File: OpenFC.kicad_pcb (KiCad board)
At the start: 8 copper layers, 28.4 x 27.6 mm, 214 parts, among them J1 5V, J10 5V, J11 5V, J12 5V, J13 5V, J14 5V, J15 5V, J16 5V, J17 5V, J18 5V, J19 5V, J2 5V, J20 5V, J21 5V, J22 5V, J23 5V, J24 5V, J25 5V, J26 5V, J27 5V, J28 5V, J29 5V, J3 5V, J30 5V, J31 5V, J32 5V, J33 5V, J34 5V, J35 5V, J36 5V, J38 5V, J39 5V, J4 5V, J40 5V, J42 5V, J43 5V, J44 5V, J45 5V, J46 5V, J47 5V, J48 5V, J49 5V, J5 5V, J50 5V, J53 5V, J56 5V, J6 5V, J7 5V, J8 5V, J9 5V, P1 SM08B-SRSS-TB(LF)(SN), Q7 DMN1150UFB-7B, U1 SM06B-SRSS-TB(LF)(SN), U10 GD25Q256EWIGR, U12 WL9005D4-33, U13 TPS746-3.3DRV, U14 LSM6DSV16XTR, U15 XL-1010RGBC-WS2812B, U16 XL-1010RGBC-WS2812B, U17 XL-1010RGBC-WS2812B, U18 XL-1010RGBC-WS2812B, U19 XL-1010RGBC-WS2812B, U2 ESP32-C3FH4, U20 SX1281IMLTRT, U21 TPS746-3.3DRV, U22 XL-1010RGBC-WS2812B, U23 XL-1010RGBC-WS2812B, U24 XL-1010RGBC-WS2812B, U25 XL-1010RGBC-WS2812B, U26 XL-1010RGBC-WS2812B, U27 XL-1010RGBC-WS2812B, U28 XL-1010RGBC-WS2812B, U29 XL-1010RGBC-WS2812B, U3 XL-1010RGBC-WS2812B, U30 BMP388, U32 RP2354A, U33 TPS2116DRLR, U34 TS2306A 240GF MSM 9_C2976675, U35 STM32G431KBUx, U4 XL-1010RGBC-WS2812B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

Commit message: Ordered first revision
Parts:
- removed C61, C64, C65, C66: 100n, Capacitor_SMD:C_0402_1005Metric
- removed D8: LED_1_Green, LED_SMD:LED_0603_1608Metric
- removed R21: 33R, Resistor_SMD:R_0402_1005Metric
- removed U21: TPS746-3.3DRV, Package_SON:WSON-6-1EP_2x2mm_P0.65mm_EP1x1.6mm
- removed X2: Q22FA12800519, lib:CRYSTAL-SMD_4P-L2.0-W1.6-BL
- added D7: LED_1_Green, LED_SMD:LED_0603_1608Metric, F.Cu at (57.0, 105.9)
- added OSC1: OW7EL89CENUNFAYLC-52M, lib:OSC-SMD_4P-L2.0-W1.6-BL_TXC_7Z, F.Cu at (70.2, 114.3)
- added Q1: DMN1150UFB-7B, lib:DFN-3L_L1.0-W0.6-P0.65-BR, F.Cu at (58.0, 105.8)
- added R12: 200R, Resistor_SMD:R_0402_1005Metric, B.Cu at (56.5, 104.7)
- added U11: LP5900SDX-1.8/NOPB, lib:WSON-6_L2.5-W2.2-P0.65-BL-EP, B.Cu at (58.4, 106.5)
- C11, C44, C49, C75, L1, Q7, R2, R36: moved to F.Cu
- C19, C36, C45, D21, R14, R15: moved to B.Cu
- C59: value 100n -> 15p; moved to F.Cu
- FL1, FL2: value 2450FM07D0034T -> DEA102700LT-6307A2
- R17, R18: value 22R -> 30R
- R19, R4: value 33R -> 30R
- R23, R24: value 5.1k -> 6.8k
- moved R29 20.2 mm to (56.4, 102.9), turned to 180 degrees
- moved C49 20.1 mm to (50.9, 120.2), turned to -135 degrees
- moved R31 17.1 mm to (60.0, 116.6), turned to -90 degrees
- moved L4 16.9 mm to (65.8, 115.6), turned to 0 degrees
- moved R16 16.4 mm to (59.5, 118.0)
- moved C37 15.4 mm to (62.5, 117.6), turned to 180 degrees
- moved R34 13.6 mm to (68.0, 102.1), turned to 90 degrees
- moved C39 13.1 mm to (60.0, 114.8), turned to 90 degrees
- moved R22 13.0 mm to (56.4, 102.0), turned to 0 degrees
- moved R10 12.4 mm to (67.1, 102.1), turned to 90 degrees
- moved C40 12.2 mm to (64.5, 113.4), turned to 180 degrees
- moved U7 11.6 mm to (62.3, 115.4), turned to -90 degrees
- moved R37 11.3 mm to (57.9, 104.2), turned to 0 degrees
- moved R5 9.69 mm to (65.3, 115.9), turned to 180 degrees
- moved C45 9.43 mm to (64.3, 105.0), turned to 0 degrees
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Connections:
- net +3.3V_GYRO renamed +1.8V_GYRO
- C59 pad 1: +3.3V -> GND
- C59 pad 2: GND -> Net-(OSC1-Out_Put)
- C60 pad 1: +3.3V -> +3.3V_ELRS
- P1 pad 10: unconnected-(P1-Pad10) -> GND
- P1 pad 9: unconnected-(P1-Pad9) -> GND
- U1 pad 7: unconnected-(U1-Pad7) -> GND
- U1 pad 8: unconnected-(U1-Pad8) -> GND
- U2 pad 24: /ELRS/MOSI -> unconnected-(U2-SPIQ-Pad24)
- U2 pad 4: unconnected-(U2-XTAL_32K_P-Pad4) -> /ELRS/DIO
- U20 pad 4: Net-(U20-XTA) -> Net-(OSC1-Out_Put)
- U20 pad 6: Net-(U20-XTB) -> unconnected-(U20-XTB-Pad6)
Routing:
- net /OSD/OSD_TX: track 1.46 -> 35.7 mm, vias 1 -> 2
- net GND: track 124.4 -> 92.4 mm, vias 91 -> 80
- net +12V: track 9.12 -> 40.4 mm, vias 4 -> 6
- net Net-(D5-A): track 33.5 -> 5.62 mm, vias 2 -> 1
- net /ELRS/ESP_BOOT0: track 1.36 -> 25.5 mm, vias 1 -> 3
- net +BATT: track 70.4 -> 46.8 mm, vias 7 -> 6
- net +5V_BUCK: track 24.2 -> 45.9 mm, vias 5 -> 8
- net Net-(D6-A): track 28.7 -> 7.34 mm, vias 2 -> 1
- net /ELRS/ESP8285_EN: track 2.11 -> 19.9 mm, vias 1 -> 2
- net /RP2350A/LED0: track 2.06 -> 18.2 mm, vias 1 -> 2
- net Net-(Q7-G): track 16.0 -> 1.97 mm, vias 2 -> 0
- net /RP2350A/Motor4: track 36.5 -> 25.1 mm, vias 2 -> 3
- net /RP2350A/D-_C: track 2.47 -> 13.5 mm
- net /I2C_SCL: track 29.9 -> 20.5 mm
- net /PADS/SBUS: track 23.3 -> 15.3 mm, vias 2 -> 3
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- added copper zone on In3.Cu, net +3.3V_ELRS
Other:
- board size 28.4 x 27.6 mm -> 27.6 x 27.6 mm
- board text added: "LN4 = Signal"
- board text added: "OPENFC"
- board text added: "power?"
- board text removed: "LN4 = GND"
- board text removed: "antenna"
- board text removed: "break me"

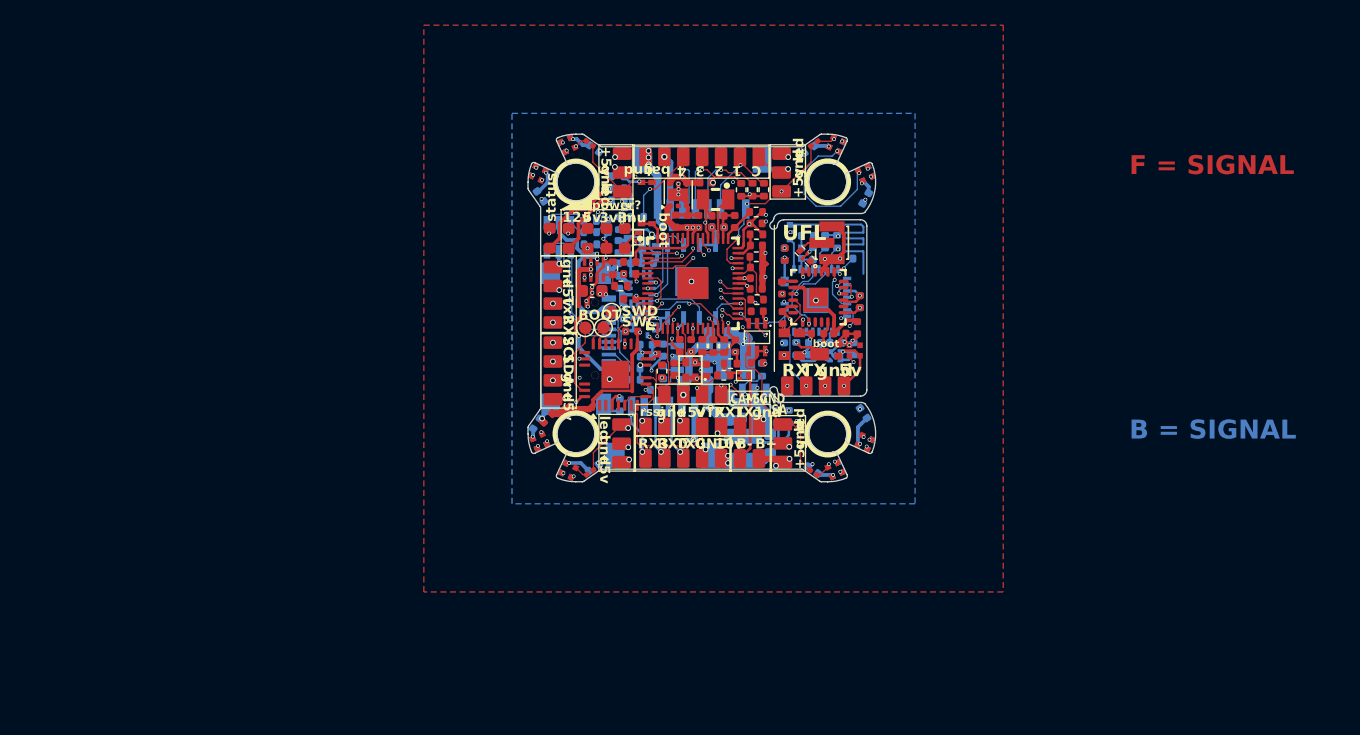
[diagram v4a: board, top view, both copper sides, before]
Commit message: Switched to RP2354B for V2 of the FC for more IO. I want to try implement OSD on PIO state machine. I know BF already uses all of them but it should be possible and then later try to combine it witht the WS2812 protocol PIO2. If anybody here has any experience with analog OSD generation let me know, I just want to make a circuit that would allow further software development later. The reason I want to do it this way is it's cheap BOM<1 euro and low footprint, just 2 2x2 IC's and some passives.
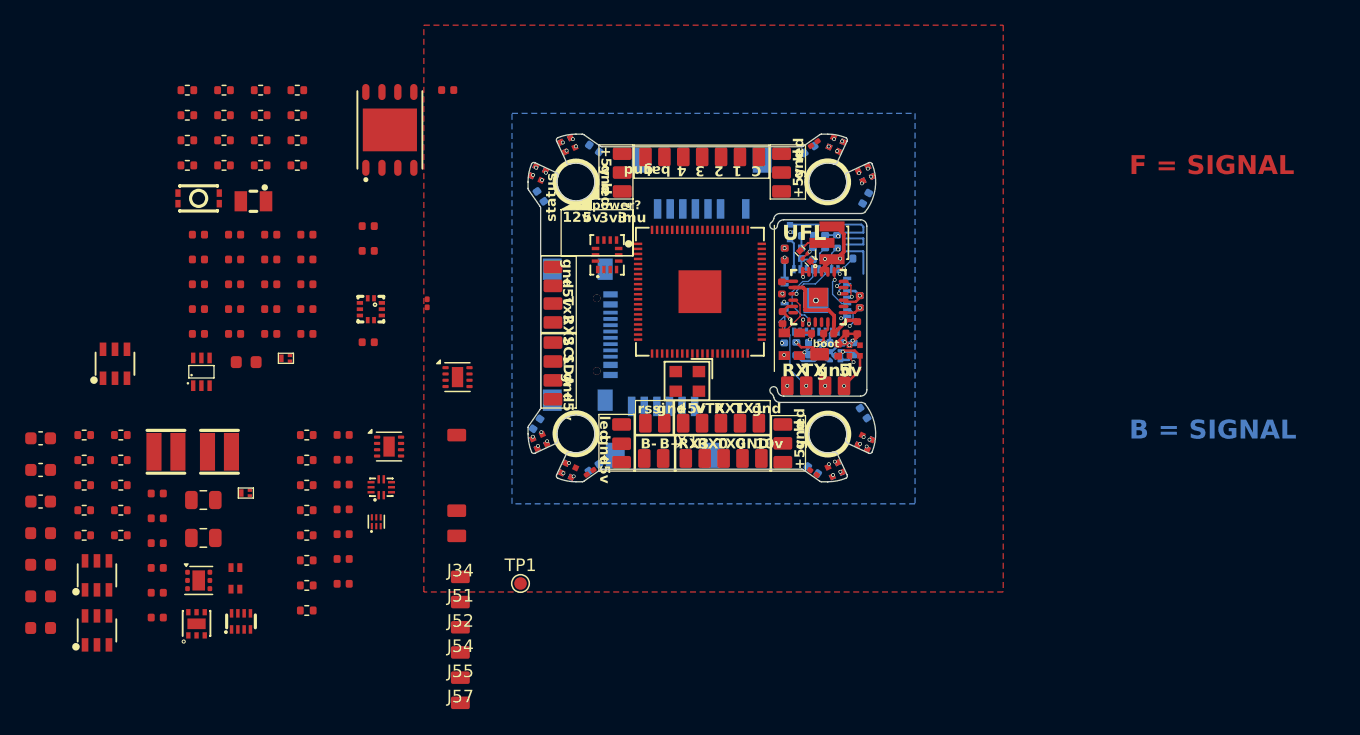
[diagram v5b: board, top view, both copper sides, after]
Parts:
- removed C10, C15, C2, C20, C24, C25, C26, C27, C28, C29, C30, C31, C4, C42, C44, C69: 100n, Capacitor_SMD:C_0402_1005Metric
- removed C21, C22, C23, C6: 4.7uF, Capacitor_SMD:C_0402_1005Metric
- removed C3: 15p, Capacitor_SMD:C_0402_1005Metric
- removed D2: USBLC6-2SC6, lib:SOT-23-6_L2.9-W1.6-P0.95-LS2.8-BL
- removed L2: AOTA-B201610S3R3-101-T, lib:IND-SMD_L2.0-W1.6_AOTA-B201610S3R3-101-T
- removed R10, R23, R24, R34, R36, R37: 6.8k, Resistor_SMD:R_0402_1005Metric
- removed R11, R25, R26: 10k, Resistor_SMD:R_0402_1005Metric
- removed R17, R18, R19: 30R, Resistor_SMD:R_0402_1005Metric
- removed R20: 200R, Resistor_SMD:R_0402_1005Metric
- removed R44, R45: 5.1k, Resistor_SMD:R_0402_1005Metric
- removed R50: 100k, Resistor_SMD:R_0402_1005Metric
- removed TP2, TP3: TestPoint, TestPoint:TestPoint_Pad_D1.0mm
- removed U10: GD25Q256EWIGR, lib:WSON-8_L6.0-W5.0-P1.27-TL-EP
- removed U11: LP5900SDX-1.8/NOPB, lib:WSON-6_L2.5-W2.2-P0.65-BL-EP
- removed U32: RP2354A, lib:QFN-60_L7.0-W7.0-P0.40-TL-EP3.4
- removed U34: TS2306A 240GF MSM 9_C2976675, lib:SW-SMD_4P-L3.0-W2.0-P0.85-LS3.5
- removed USB2: TYPE-C 16P QTWT, lib:USB-TYPE-C-SMD_TYPE-C-16P-QTWT
- removed X3: OT4EL89CJI-111YLC-12M, lib:OSC-SMD_4P-L1.6-W1.2-BL-1
- added C61: 100n, Capacitor_SMD:C_0402_1005Metric, F.Cu at (34.6, 123.5)
- added C62: 100n, Capacitor_SMD:C_0402_1005Metric, F.Cu at (34.6, 125.5)
- added C63: 100n, Capacitor_SMD:C_0402_1005Metric, F.Cu at (34.6, 127.4)
- added C64: 100n, Capacitor_SMD:C_0402_1005Metric, F.Cu at (34.6, 129.4)
- added C65: 100n, Capacitor_SMD:C_0402_1005Metric, F.Cu at (34.6, 131.4)
- added C66: 100n, Capacitor_SMD:C_0402_1005Metric, F.Cu at (34.6, 133.3)
- added C67: 4.7uF, Capacitor_SMD:C_0402_1005Metric, F.Cu at (23.1, 105.6)
- added C68: 4.7uF, Capacitor_SMD:C_0402_1005Metric, F.Cu at (23.1, 107.6)
- added C70: 100n, Capacitor_SMD:C_0402_1005Metric, F.Cu at (23.1, 109.6)
- added C72: 100n, Capacitor_SMD:C_0402_1005Metric, F.Cu at (23.1, 113.5)
- added C73: 20p, Capacitor_SMD:C_0402_1005Metric, F.Cu at (26.0, 105.6)
- added C74: 20p, Capacitor_SMD:C_0402_1005Metric, F.Cu at (26.0, 107.6)
- added C77: 4.7uF, Capacitor_SMD:C_0402_1005Metric, F.Cu at (26.0, 113.5)
- added C78: 100n, Capacitor_SMD:C_0402_1005Metric, F.Cu at (28.8, 105.6)
- added C79: 100n, Capacitor_SMD:C_0402_1005Metric, F.Cu at (28.8, 107.6)
- added C80: 100n, Capacitor_SMD:C_0402_1005Metric, F.Cu at (28.8, 109.6)
- added C81: 100n, Capacitor_SMD:C_0402_1005Metric, F.Cu at (28.8, 111.5)
- added C82: 100n, Capacitor_SMD:C_0402_1005Metric, F.Cu at (28.8, 113.5)
- added C83: 100n, Capacitor_SMD:C_0402_1005Metric, F.Cu at (31.7, 105.6)
- added C84: 100n, Capacitor_SMD:C_0402_1005Metric, F.Cu at (31.7, 107.6)
- added C85: 100n, Capacitor_SMD:C_0402_1005Metric, F.Cu at (31.7, 109.6)
- added C86: 100n, Capacitor_SMD:C_0402_1005Metric, F.Cu at (31.7, 111.5)
- added C87: 100n, Capacitor_SMD:C_0402_1005Metric, F.Cu at (31.7, 113.5)
- added D8: USBLC6-2SC6, lib:SOT-23-6_L2.9-W1.6-P0.95-LS2.8-BL, F.Cu at (16.5, 115.9)
- added J51: 5V, lib:small_pad, F.Cu at (43.9, 134.8)
- added J52: 5V, lib:small_pad, F.Cu at (43.9, 136.8)
- added J54: 5V, lib:small_pad, F.Cu at (43.9, 138.8)
- added J55: 5V, lib:small_pad, F.Cu at (43.9, 140.8)
- added J57: 5V, lib:small_pad, F.Cu at (43.9, 142.8)
- added R27: 33R, Resistor_SMD:R_0402_1005Metric, F.Cu at (31.7, 123.5)
- added R30: 1k, Resistor_SMD:R_0402_1005Metric, F.Cu at (31.7, 125.5)
- added R32: 33R, Resistor_SMD:R_0402_1005Metric, F.Cu at (31.7, 127.5)
- added R33: 1k, Resistor_SMD:R_0402_1005Metric, F.Cu at (31.7, 129.5)
- added R35: 150k, Resistor_SMD:R_0402_1005Metric, F.Cu at (31.7, 131.5)
- added R38: 10k, Resistor_SMD:R_0402_1005Metric, F.Cu at (31.7, 133.5)
- added R39: 4.7k, Resistor_SMD:R_0402_1005Metric, F.Cu at (31.7, 135.5)
- added R40: 10k, Resistor_SMD:R_0402_1005Metric, F.Cu at (22.2, 100.1)
- added R42: 6.8k, Resistor_SMD:R_0402_1005Metric, F.Cu at (25.1, 94.2)
- added R43: 6.8k, Resistor_SMD:R_0402_1005Metric, F.Cu at (25.1, 96.2)
- added R46: 100k, Resistor_SMD:R_0402_1005Metric, F.Cu at (25.1, 98.1)
- added R47: 10k, Resistor_SMD:R_0402_1005Metric, F.Cu at (25.1, 100.1)
- added R48: 30R, Resistor_SMD:R_0402_1005Metric, F.Cu at (28.0, 94.2)
- added R49: 30R, Resistor_SMD:R_0402_1005Metric, F.Cu at (28.0, 96.2)
- added R51: 5.1k, Resistor_SMD:R_0402_1005Metric, F.Cu at (28.0, 98.1)
- added R52: 5.1k, Resistor_SMD:R_0402_1005Metric, F.Cu at (28.0, 100.1)
- added R53: 1k, Resistor_SMD:R_0402_1005Metric, F.Cu at (31.0, 94.2)
- added R54: 10k, Resistor_SMD:R_0402_1005Metric, F.Cu at (31.0, 96.2)
- added R55: 200R, Resistor_SMD:R_0402_1005Metric, F.Cu at (31.0, 98.1)
- added R56: 30R, Resistor_SMD:R_0402_1005Metric, F.Cu at (31.0, 100.1)
- added U21: NCV8187AMT180TAG, lib:WDFN-6_L2.0-W2.0-P0.65-BL-EP, F.Cu at (23.0, 136.5)
- added U36: RP2354B_C39843328, lib:QFN-80_L10.0-W10.0-P0.40-TL-EP3.4, F.Cu at (62.9, 110.2)
- added U37: TLV9062IDSGR, Package_SON:WSON-8-1EP_2x2mm_P0.5mm_EP0.9x1.6mm, F.Cu at (38.2, 122.5)
- added U38: LM393LVDSGR, Package_SON:WSON-8-1EP_2x2mm_P0.5mm_EP0.9x1.6mm, F.Cu at (43.7, 116.9)
- added U39: 74LVC1G66, lib:TDFN-6_L1.0-W1.0-P0.35-BL, F.Cu at (37.2, 128.4)
- added U41: TS2306A 240GF MSM 9_C2976675, lib:SW-SMD_4P-L3.0-W2.0-P0.85-LS3.5, F.Cu at (23.1, 102.8)
- added U42: TXU0101DCKR, lib:SC-70-6_L2.0-W1.3-P0.65-LS2.1-BL, F.Cu at (23.3, 116.5)
- added USB1: TYPE-C 16P QTWT, lib:USB-TYPE-C-SMD_TYPE-C-16P-QTWT, B.Cu at (53.5, 113.6)
- added X1: XTM25012000JT00351001, lib:CRYSTAL-SMD_4P-L2.5-W2.0-BL-A, F.Cu at (61.9, 117.3)
- C111, C34, C35, C36, C37, C38, C39, C40, C41, C45, C76, D21, L3, L4, R12, R14, R15, R16, R22, R28, R29, R31, R4, U14, U30, U6, U7: moved to F.Cu
- C33: value 100n -> 1uF; moved to F.Cu
- C43: value 22uF -> 10uF; moved to F.Cu
- C71: value 100n -> 4.7uF; moved to F.Cu
- L1: value BLM15AG601SN1D -> AOTA-B201610S3R3-101-T; footprint lib:L0402 -> lib:IND-SMD_L2.0-W1.6_AOTA-B201610S3R3-101-T
- R2: value 75 -> 1M
- U35: value STM32G431KBUx -> FSUSB42UMX; footprint Package_DFN_QFN:QFN-32-1EP_5x5mm_P0.5mm_EP3.1x3.1mm -> lib:UMLP-10_L1.8-W1.4-P0.40-BL
- U9: value TXU0101DCKR -> BY25Q128ASWIG(R); footprint lib:SC-70-6_L2.0-W1.3-P0.65-LS2.1-BL -> lib:WSON-8_L6.0-W5.0-P1.27-BL-EP
- moved C38 57.9 mm to (10.6, 121.8), turned to 0 degrees
- moved R14 56.7 mm to (14.0, 129.5), turned to 0 degrees
- moved D7 55.7 mm to (10.6, 136.9), turned to 0 degrees
- moved C40 55.0 mm to (10.6, 124.3), turned to 0 degrees
- moved U6 53.9 mm to (15.1, 132.7), turned to 0 degrees
- moved U7 51.9 mm to (15.1, 137.1), turned to 0 degrees
- moved D4 51.9 mm to (10.6, 131.8), turned to 0 degrees
- moved R28 51.7 mm to (16.9, 125.5), turned to 0 degrees
- moved C32 51.1 mm to (19.8, 128.2)
- moved D5 50.7 mm to (10.6, 134.3), turned to 0 degrees
- moved C36 50.6 mm to (19.8, 132.1), turned to 0 degrees
- moved D1 49.3 mm to (10.6, 129.3), turned to 0 degrees
- moved U13 48.9 mm to (23.1, 133.1), turned to 0 degrees
- moved R5 48.3 mm to (22.2, 94.2), turned to 0 degrees
- moved R12 48.2 mm to (14.0, 127.5), turned to 0 degrees
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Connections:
- net /RP2350A/Motor1 renamed /PADS/M1
- net /RP2350A/Motor2 renamed /PADS/M2
- net /RP2350A/Motor3 renamed /PADS/M3
- net /RP2350A/Motor4 renamed /PADS/M4
- C71 pad 1: Net-(U35-VDDA) -> Net-(U36-ADC_AVDD)
- C75 pad 1: +3.3V -> +1.1V
- C76 pad 1: /OSD/NRST -> +1.1V
- J34 pad 1: /OSD/SA_OUT -> +5V
- J56 pad 1: /PADS/ADC2 -> /PADS/RSSI
- JP1 pad 1: /LED -> /LED's/LED_STRIP
- JP2 pad 1: /LED -> /LED's/LED_STRIP
- JP3 pad 1: /LED -> /LED's/LED_STRIP
- JP4 pad 1: /LED -> /LED's/LED_STRIP
- L1 pad 1: +3.3V -> +1.1V
- L1 pad 2: Net-(U35-VDDA) -> Net-(U36-VREG_LX)
- R2 pad 1: GND -> /OSD/VID_AC
- R2 pad 2: /OSD/VIDEO_IN -> GND
- TP1 pad 1: /OSD/OSD_SWD -> /RP2350A/DBG_OSD
- U14 pad 1: /BLACKBOX/SPI.MISO -> /IMU/SPI0.MISO
- U14 pad 13: /BLACKBOX/SPI.SCK -> /IMU/SPI0.SCK
- U14 pad 14: /BLACKBOX/SPI.MOSI -> /IMU/SPI0.MOSI
- U30 pad 2: /I2C_SCL -> /BAROMETER/I2C_SCL
- U30 pad 4: /I2C_SDA -> /BAROMETER/I2C_SDA
- U35 pad 1: +3.3V -> /OSD/VID_MUX_OUT
- U35 pad 2: unconnected-(U35-PF0-Pad2) -> /OSD/VID_MUX_OUT
- U35 pad 3: unconnected-(U35-PF1-Pad3) -> GND
- U35 pad 4: /OSD/NRST -> /OSD/VWHITE_BUF
- U35 pad 5: unconnected-(U35-PA0-Pad5) -> /OSD/VWHITE_BUF
- U35 pad 6: Net-(U35-PA1) -> /OSD/VID_BUF
- U35 pad 7: /OSD/VIDEO_OUT -> /OSD/VID_BUF
- U35 pad 8: Net-(U35-PA3) -> GND
- U35 pad 9: Net-(U35-PA1) -> +3.3V
- U9 pad 1: +3.3V -> /BLACKBOX/BB_CS
- U9 pad 2: GND -> /BLACKBOX/SPI1.MISO
- U9 pad 3: /RP2350A/LED_STRIP_L -> +3.3V
- U9 pad 4: /LED -> GND
- U9 pad 5: +5V -> /BLACKBOX/SPI1.MOSI
- U9 pad 6: +5V -> /BLACKBOX/SPI1.SCK
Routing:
- net /LED: track 70.5 -> 0.00 mm, vias 6 -> 0
- net GND: track 92.4 -> 25.4 mm, vias 80 -> 25
- net +3.3V: track 60.8 -> 0.00 mm, vias 18 -> 0
- net +BATT: track 46.8 -> 0.00 mm, vias 6 -> 0
- net +5V: track 59.1 -> 13.1 mm, vias 26 -> 10
- net +5V_BUCK: track 45.9 -> 0.00 mm, vias 8 -> 0
- net +12V: track 40.4 -> 0.00 mm, vias 6 -> 0
- net /OSD/OSD_TX: track 35.7 -> 0.00 mm, vias 2 -> 0
- net +1.1V: track 32.0 -> 0.00 mm, vias 4 -> 0
- net /PADS/M1: track 26.5 -> 0.00 mm, vias 2 -> 0
- net /PADS/M2: track 25.4 -> 0.00 mm, vias 2 -> 0
- net /PADS/M4: track 25.1 -> 0.00 mm, vias 3 -> 0
- net /PADS/M3: track 25.1 -> 0.00 mm, vias 2 -> 0
- net /PADS/DIGITAL_TX: track 23.9 -> 0.00 mm, vias 3 -> 0
- net /PADS/DIGITAL_RX: track 23.5 -> 0.00 mm, vias 3 -> 0
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- removed copper zone on In3.Cu, net +3.3V
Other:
- board text removed: "BOOT"
- board text removed: "CAM"
- board text removed: "ELRS"
- board text removed: "OPENFC"
- board text removed: "SA"
- board text removed: "SWC"
- board text removed: "SWD"
